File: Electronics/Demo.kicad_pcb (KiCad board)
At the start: 2 copper layers, 61 x 49 mm, 27 parts, among them J1 RJ10, J2 RJ10, J3 Conn_01x02_Male, J4 PWR, SW1 SW_Push, SW2 SW_Push, SW3 SW_Push, U1 MCP2551-I-SN, U2 MCP2515-xSO, Y1 8MHz

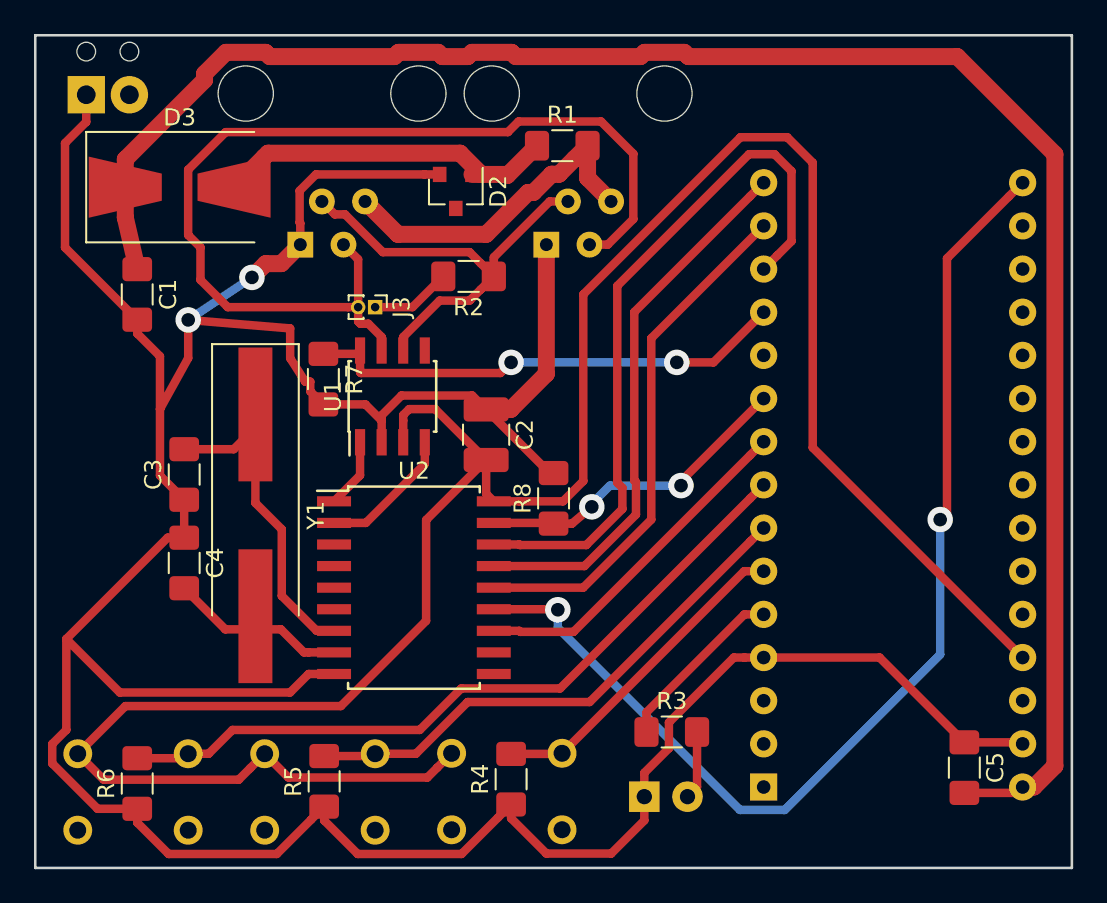
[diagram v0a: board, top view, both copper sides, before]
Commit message: Updated footprints and routing.
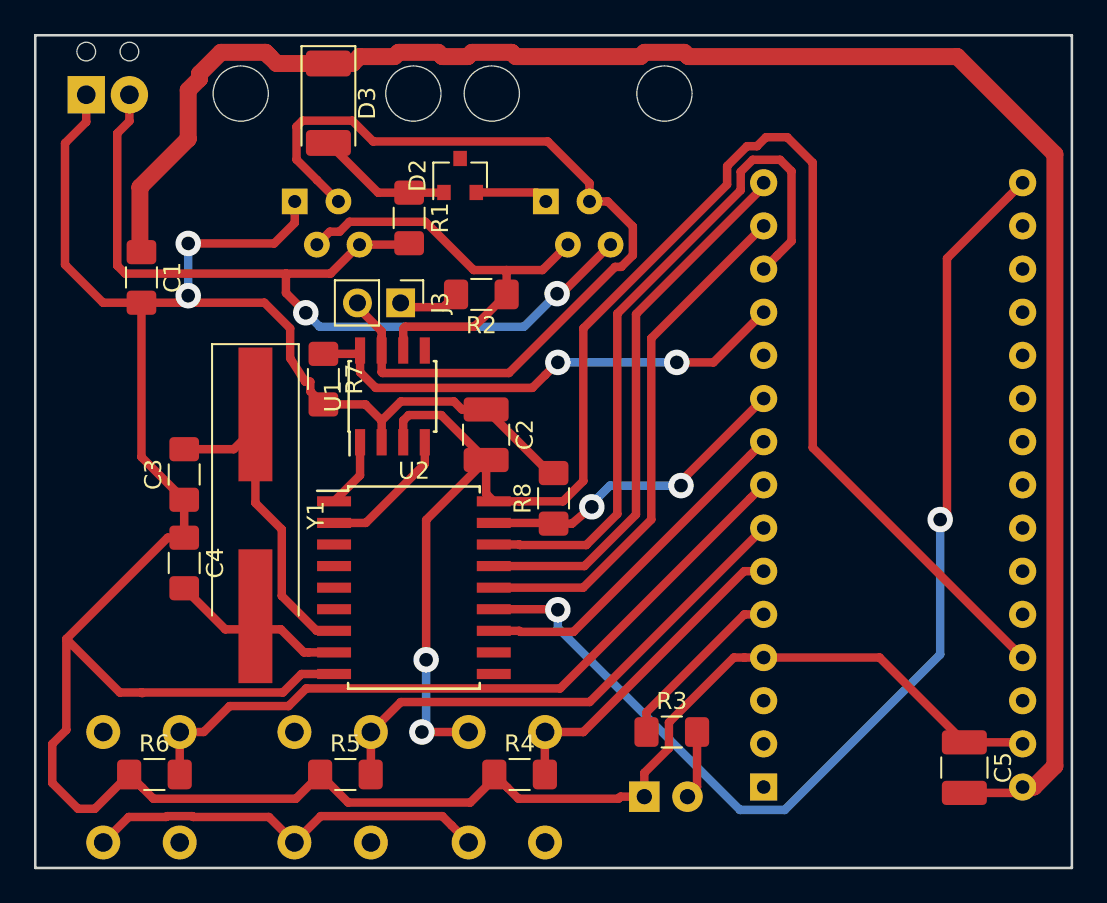
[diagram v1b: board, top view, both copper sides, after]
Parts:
- C5: footprint Capacitor_SMD:C_1206_3216Metric_Pad1.42x1.75mm_HandSolder -> Capacitor_SMD:C_1210_3225Metric_Pad1.42x2.65mm_HandSolder
- D3: footprint Diode_SMD:D_SMB-SMC_Universal_Handsoldering -> Diode_SMD:D_2010_5025Metric_Pad1.52x2.65mm_HandSolder
- J1, J2: footprint Controller-Local:RJ14 -> Demo:RJ14
- J3: footprint Connector_PinHeader_1.00mm:PinHeader_1x02_P1.00mm_Vertical -> Connector_PinHeader_2.54mm:PinHeader_1x02_P2.54mm_Vertical
- SW1, SW2, SW3: footprint Button_Switch_THT:SW_TH_Tactile_Omron_B3F-10xx -> Button_Switch_THT:SW_PUSH_6mm_H4.3mm
- moved D3 10.1 mm to (140.2, 86.0), turned to 270 degrees
- moved R1 9.96 mm to (145.0, 92.8), turned to 270 degrees
- moved SW1 5.34 mm to (153.0, 129.5), turned to 90 degrees
- moved SW3 5.25 mm to (131.5, 129.5), turned to 90 degrees
- moved SW2 5.23 mm to (142.8, 129.5), turned to 90 degrees
- moved J3 1.52 mm to (144.5, 97.8)
- moved R5 1.31 mm to (141.2, 125.5), turned to 0 degrees
- moved R2 1.30 mm to (149.2, 97.2)
- moved R6 1.14 mm to (130.0, 125.5), turned to 0 degrees
- moved C1 1.03 mm to (129.2, 96.2)
- moved D2 0.97 mm to (148.0, 90.2), turned to 90 degrees
- moved R4 0.57 mm to (151.5, 125.5), turned to 0 degrees
- moved J1 0.30 mm to (137.0, 94.3)
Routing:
- net /Vin: track 19.9 -> 51.5 mm, vias 0 -> 2
- net GND: track 207.3 -> 185.1 mm
- net +5V: track 138.5 -> 122.8 mm, vias 0 -> 2
- net Net-(D2-Pad1): track 20.5 -> 8.02 mm
- net /CANH: track 59.4 -> 52.9 mm
- net Net-(J3-Pad1): track 4.76 -> 3.57 mm
- net /CANL: track 26.4 -> 27.6 mm
- net /CS: track 42.0 -> 41.2 mm
- net /S2: track 31.4 -> 30.6 mm
- net /XCDR_RST: track 28.8 -> 29.5 mm
- net /S3: track 43.5 -> 42.9 mm
- net +12V: track 108.7 -> 108.1 mm
